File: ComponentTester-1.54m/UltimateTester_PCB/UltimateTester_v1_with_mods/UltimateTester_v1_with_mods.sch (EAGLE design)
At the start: 139 parts, among them IC1 MT3608, IC1-BATT-PROTECT XB8089D, IC2-CHARGER BQ21040DB, IC3 MT3608, IC4-E-FUSE TPS259630, IC5-5V LP2992IM5-5.0, J1 USB-A-RECEPTABLE, U1 ATMEGA328P-AU-TQFP, U2 INA226AIDGST

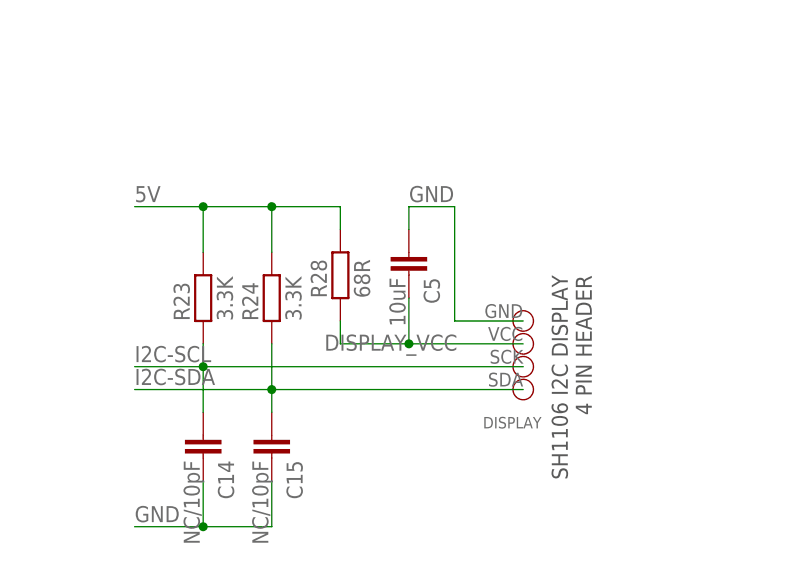
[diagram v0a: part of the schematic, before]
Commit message: Add SSD1309 1.54 inch OLED I2C Display
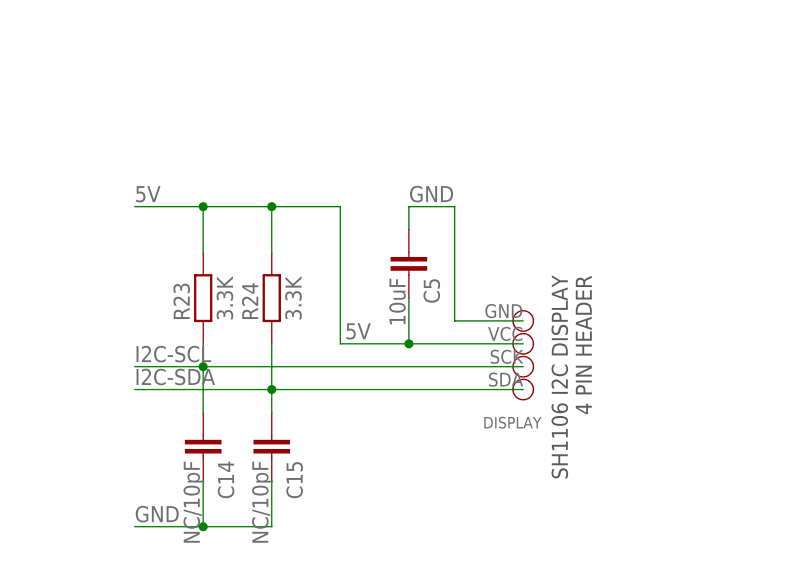
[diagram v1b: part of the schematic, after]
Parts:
- removed R28: 68R, .MyComponents:RESISTOR_SMD0603
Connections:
- removed net DISPLAY_VCC: C5.1, DISPLAY.VCC, R28.1
- net 5V: now also C5.1, DISPLAY.VCC; no longer R28.2
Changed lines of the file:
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@@
 <part name="C14" library=".MyComponents" deviceset="CAPACITOR_SMD" device="0603" value="NC/10pF"/>
 <part name="C15" library=".MyComponents" deviceset="CAPACITOR_SMD" device="0603" value="NC/10pF"/>
-<part name="R28" library=".MyComponents" deviceset="RESISTOR_SMD" device="0603" value="68R"/>
 <part name="GND2" library=".MyComponents" deviceset="TEST-POINT" device="-TH"/>
 <part name="20MHZ" library=".MyComponents" deviceset="CRYSTAL-20MHZ-ECS-200-18-4X-CKM" device="" value="ECS-200-18-4X-CKM"/>
@@
 <attribute name="VALUE" x="-174.879" y="-56.134" size="1.778" layer="96" rot="R270"/>
 </instance>
-<instance part="R28" gate="G$1" x="-165.1" y="-35.56" smashed="yes" rot="R90" grouprefs="DISPLAY_GRP">
-<attribute name="NAME" x="-166.5986" y="-38.1" size="1.778" layer="95" rot="R90"/>
-<attribute name="VALUE" x="-161.798" y="-38.1" size="1.778" layer="96" rot="R90"/>
-</instance>
 <instance part="GND2" gate="G$1" x="200.66" y="10.16" smashed="yes" grouprefs="5-BOOST-GRP-VOUT">
 <attribute name="NAME" x="201.422" y="11.684" size="1.778" layer="95" rot="R90"/>
@@
 <junction x="-172.72" y="-27.94" grouprefs="DISPLAY_GRP"/>
 <label x="-187.96" y="-27.432" size="1.778" layer="95" grouprefs="DISPLAY_GRP"/>
-<wire x1="-165.1" y1="-30.48" x2="-165.1" y2="-27.94" width="0.1524" layer="91" grouprefs="DISPLAY_GRP"/>
 <pinref part="R24" gate="G$1" pin="2"/>
 <pinref part="R23" gate="G$1" pin="2"/>
-<pinref part="R28" gate="G$1" pin="2"/>
+<wire x1="-157.48" y1="-43.18" x2="-157.48" y2="-38.1" width="0.1524" layer="91" grouprefs="DISPLAY_GRP"/>
+<wire x1="-157.48" y1="-43.18" x2="-165.1" y2="-43.18" width="0.1524" layer="91" grouprefs="DISPLAY_GRP"/>
+<junction x="-157.48" y="-43.18" grouprefs="DISPLAY_GRP"/>
+<wire x1="-144.78" y1="-43.18" x2="-157.48" y2="-43.18" width="0.1524" layer="91" grouprefs="DISPLAY_GRP"/>
+<label x="-164.592" y="-42.672" size="1.778" layer="95" grouprefs="DISPLAY_GRP"/>
+<pinref part="DISPLAY" gate="G$1" pin="VCC"/>
+<pinref part="C5" gate="G$1" pin="1"/>
+<wire x1="-165.1" y1="-27.94" x2="-165.1" y2="-43.18" width="0.1524" layer="91"/>
 </segment>
 <segment>
@@
 </segment>
 </net>
-<net name="DISPLAY_VCC" class="0">
-<segment>
-<wire x1="-157.48" y1="-43.18" x2="-157.48" y2="-38.1" width="0.1524" layer="91" grouprefs="DISPLAY_GRP"/>
-<wire x1="-157.48" y1="-43.18" x2="-165.1" y2="-43.18" width="0.1524" layer="91" grouprefs="DISPLAY_GRP"/>
-<junction x="-157.48" y="-43.18" grouprefs="DISPLAY_GRP"/>
-<wire x1="-144.78" y1="-43.18" x2="-157.48" y2="-43.18" width="0.1524" layer="91" grouprefs="DISPLAY_GRP"/>
-<label x="-166.878" y="-43.942" size="1.778" layer="95" grouprefs="DISPLAY_GRP"/>
-<wire x1="-165.1" y1="-40.64" x2="-165.1" y2="-43.18" width="0.1524" layer="91" grouprefs="DISPLAY_GRP"/>
-<pinref part="DISPLAY" gate="G$1" pin="VCC"/>
-<pinref part="C5" gate="G$1" pin="1"/>
-<pinref part="R28" gate="G$1" pin="1"/>
-</segment>
-</net>
